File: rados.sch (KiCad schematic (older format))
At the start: 1 part

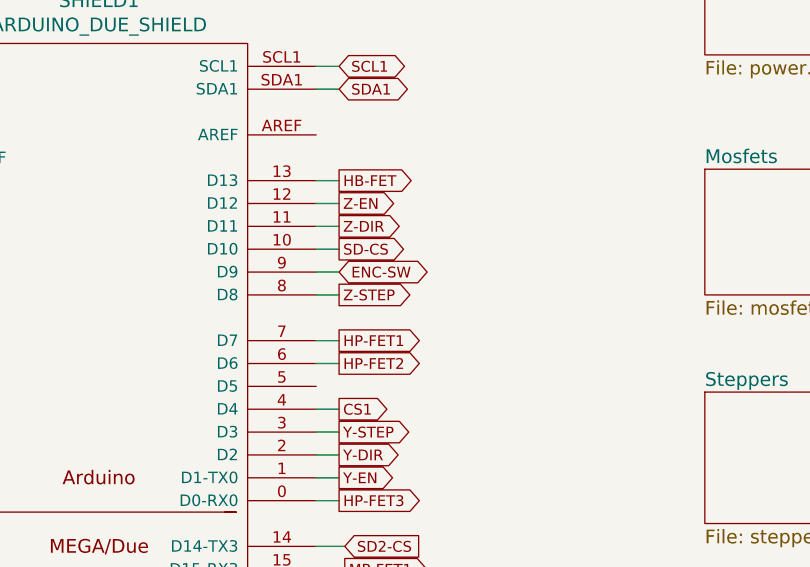
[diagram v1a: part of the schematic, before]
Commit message: Moved heatbed io away from arduino led-output (D13)
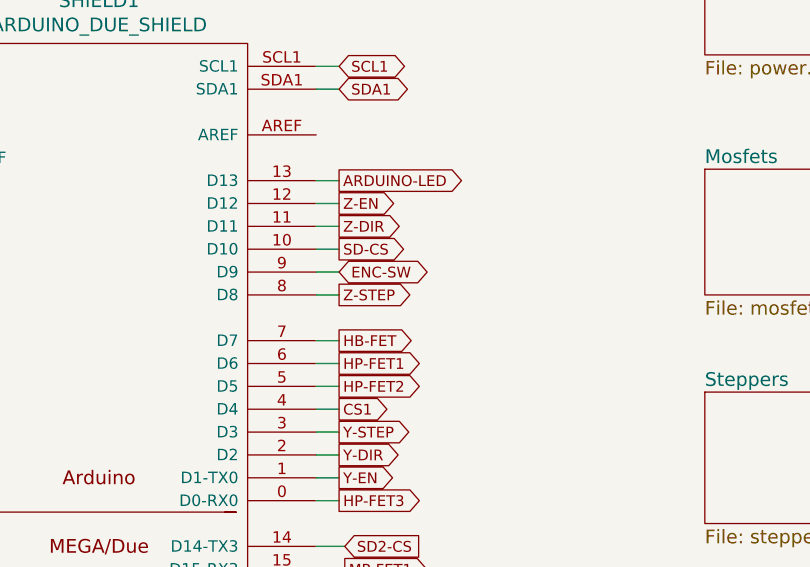
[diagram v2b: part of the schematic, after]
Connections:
- net labels added: ARDUINO-LED
- wire segments 79 -> 80
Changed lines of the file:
@@
 	1    0    0    -1
 $EndComp
-Wire Wire Line
-	2650 2300 3100 2300
 $Comp
 L +5V #PWR1
@@
 	1    0    0    -1
 $EndComp
-Wire Wire Line
-	2525 2400 3100 2400
 $Sheet
 S 6700 900  1025 550
@@
 F1 "mosfets.sch" 60
 $EndSheet
-Text GLabel 5100 2000 2    47   Output ~ 0
+Text GLabel 5100 2700 2    47   Output ~ 0
 HB-FET
-Text GLabel 5100 2700 2    47   Output ~ 0
+Text GLabel 5100 2800 2    47   Output ~ 0
 HP-FET1
-Text GLabel 5100 2800 2    47   Output ~ 0
+Text GLabel 5100 2900 2    47   Output ~ 0
 HP-FET2
 Text GLabel 5100 3400 2    47   Output ~ 0
@@
 Text GLabel 5125 4300 2    47   Output ~ 0
 LP-FET2
-Wire Wire Line
-	5000 2000 5100 2000
-Wire Wire Line
-	5000 2100 5100 2100
-Wire Wire Line
-	5000 2200 5100 2200
-Wire Wire Line
-	5000 2400 5100 2400
-Wire Wire Line
-	5000 2500 5100 2500
-Wire Wire Line
-	5000 3400 5100 3400
-Wire Wire Line
-	5100 2800 5000 2800
 $Sheet
 S 6700 2925 1050 575
@@
 Text GLabel 5100 3000 2    47   Output ~ 0
 CS1
-Wire Wire Line
-	5100 3000 5000 3000
-Wire Wire Line
-	5100 2300 5000 2300
 Text GLabel 5100 2200 2    47   Output ~ 0
 Z-DIR
 Text GLabel 5100 2500 2    47   Output ~ 0
 Z-STEP
-Wire Wire Line
-	5000 3100 5100 3100
-Wire Wire Line
-	5000 3200 5100 3200
 Text GLabel 5125 3600 2    47   Input ~ 0
 SD2-CS
@@
 	1    0    0    -1
 $EndComp
-Wire Wire Line
-	5125 3600 5000 3600
-Wire Wire Line
-	5125 3700 5000 3700
-Wire Wire Line
-	5125 3800 5000 3800
-Wire Wire Line
-	5125 3900 5000 3900
-Wire Wire Line
-	5000 4200 5125 4200
-Wire Wire Line
-	5125 4300 5000 4300
-Wire Wire Line
-	5000 4625 5000 4725
 Text GLabel 5100 3300 2    47   Output ~ 0
 Y-EN
@@
 Text GLabel 3000 6400 0    47   Input ~ 0
 Z+
-Wire Wire Line
-	5125 5050 5000 5050
-Wire Wire Line
-	5000 5250 5125 5250
-Wire Wire Line
-	5000 5450 5125 5450
-Wire Wire Line
-	5125 5150 5000 5150
-Wire Wire Line
-	5000 5550 5125 5550
-Wire Wire Line
-	5125 6000 5000 6000
-Wire Wire Line
-	5000 5350 5125 5350
-Wire Wire Line
-	5125 5650 5000 5650
-Wire Wire Line
-	5125 6200 5000 6200
 Text GLabel 5125 5900 2    47   BiDi ~ 0
 LCD-RS
@@
 Text GLabel 5125 5550 2    47   BiDi ~ 0
 ENC-A
-Wire Wire Line
-	2975 5550 3100 5550
-Wire Wire Line
-	3000 5300 3100 5300
-Wire Wire Line
-	3100 5100 3000 5100
 Text GLabel 2975 5950 0    47   Output ~ 0
 E3-EN
@@
 Text GLabel 2975 5750 0    47   Output ~ 0
 E3-DIR
-Wire Wire Line
-	3000 5000 3100 5000
-Wire Wire Line
-	3100 5200 3000 5200
-Wire Wire Line
-	3000 5450 3100 5450
 $Comp
 L GND #PWR4
@@
 	1    0    0    -1
 $EndComp
-Wire Wire Line
-	3100 4625 3100 4850
 Text GLabel 2975 3300 0    47   Output ~ 0
 E2-STEP
@@
 Text GLabel 2975 3200 0    47   Output ~ 0
 E2-DIR
-Wire Wire Line
-	2975 3400 3100 3400
-Wire Wire Line
-	3100 4000 3000 4000
-Wire Wire Line
-	3000 3900 3100 3900
 Text GLabel 2975 3000 0    47   Output ~ 0
 E1-STEP
@@
 Text GLabel 2975 2900 0    47   Output ~ 0
 E1-DIR
-Wire Wire Line
-	3000 3800 3100 3800
-Wire Wire Line
-	3100 3600 3000 3600
-Wire Wire Line
-	3000 3500 3100 3500
-Wire Wire Line
-	3000 2700 3100 2700
-Wire Wire Line
-	2650 2300 2650 2275
-Wire Wire Line
-	3000 2200 3100 2200
 Text GLabel 3000 4100 0    47   Input ~ 0
 T0
@@
 Text GLabel 3000 4500 0    47   Input ~ 0
 T4
-Wire Wire Line
-	3000 4500 3100 4500
-Wire Wire Line
-	3100 4400 3000 4400
-Wire Wire Line
-	3000 4300 3100 4300
-Wire Wire Line
-	3100 4200 3000 4200
-Wire Wire Line
-	3000 4100 3100 4100
 Text GLabel 5125 5350 2    47   Input ~ 0
 STATUS-LED
-Wire Wire Line
-	3000 6300 3100 6300
 Text GLabel 5100 1500 2    47   BiDi ~ 0
 SCL1
 Text GLabel 5100 1600 2    47   BiDi ~ 0
 SDA1
-Wire Wire Line
-	5100 1500 5000 1500
-Wire Wire Line
-	5000 1600 5100 1600
 Text GLabel 2975 1500 0    47   Input ~ 0
 SD-MISO
@@
 Text GLabel 2975 1700 0    47   Input ~ 0
 SD-SCK
-Wire Wire Line
-	2975 1500 3100 1500
-Wire Wire Line
-	3100 1600 2975 1600
-Wire Wire Line
-	2975 1700 3100 1700
-Connection ~ 3100 4725
-Connection ~ 3100 4825
-Connection ~ 5000 4625
-Wire Wire Line
-	5125 4100 5000 4100
-Wire Wire Line
-	5000 4000 5125 4000
-Wire Wire Line
-	5100 3300 5000 3300
 Text GLabel 3000 6300 0    47   Input ~ 0
 PROBE
-Wire Wire Line
-	5000 6400 5125 6400
-Wire Wire Line
-	5000 6500 5125 6500
-Wire Wire Line
-	3000 6400 3100 6400
-Wire Wire Line
-	3000 6600 3100 6600
-Wire Wire Line
-	5125 6600 5000 6600
-Wire Wire Line
-	5125 6300 5000 6300
 Text GLabel 3000 3600 0    47   BiDi ~ 0
 AUX-1
@@
 Text GLabel 3000 4000 0    47   BiDi ~ 0
 AUX-4
-Wire Wire Line
-	2975 2900 3100 2900
-Wire Wire Line
-	3100 3000 2975 3000
-Wire Wire Line
-	2975 3100 3100 3100
-Wire Wire Line
-	2975 3200 3100 3200
-Wire Wire Line
-	3100 3300 2975 3300
-Wire Wire Line
-	3000 6500 3100 6500
-Wire Wire Line
-	3100 6150 2975 6150
-Wire Wire Line
-	5125 5750 5000 5750
-Wire Wire Line
-	2975 5750 3100 5750
-Wire Wire Line
-	2975 5950 3100 5950
-Wire Wire Line
-	2975 5850 3100 5850
-Wire Wire Line
-	5100 2700 5000 2700
 Text GLabel 5125 3800 2    47   Output ~ 0
 ESP-RX
@@
 ESP-TX
 Wire Wire Line
+	2650 2300 3100 2300
+Wire Wire Line
+	2525 2400 3100 2400
+Wire Wire Line
+	5000 2700 5100 2700
+Wire Wire Line
+	5000 2100 5100 2100
+Wire Wire Line
+	5000 2200 5100 2200
+Wire Wire Line
+	5000 2400 5100 2400
+Wire Wire Line
+	5000 2500 5100 2500
+Wire Wire Line
+	5000 3400 5100 3400
+Wire Wire Line
+	5100 2900 5000 2900
+Wire Wire Line
+	5100 3000 5000 3000
+Wire Wire Line
+	5100 2300 5000 2300
+Wire Wire Line
+	5000 3100 5100 3100
+Wire Wire Line
+	5000 3200 5100 3200
+Wire Wire Line
+	5125 3600 5000 3600
+Wire Wire Line
+	5125 3700 5000 3700
+Wire Wire Line
+	5125 3800 5000 3800
+Wire Wire Line
+	5125 3900 5000 3900
+Wire Wire Line
+	5000 4200 5125 4200
+Wire Wire Line
+	5125 4300 5000 4300
+Wire Wire Line
+	5000 4625 5000 4725
+Wire Wire Line
+	5125 5050 5000 5050
+Wire Wire Line
+	5000 5250 5125 5250
+Wire Wire Line
+	5000 5450 5125 5450
+Wire Wire Line
+	5125 5150 5000 5150
+Wire Wire Line
+	5000 5550 5125 5550
+Wire Wire Line
+	5125 6000 5000 6000
+Wire Wire Line
+	5000 5350 5125 5350
+Wire Wire Line
+	5125 5650 5000 5650
+Wire Wire Line
+	5125 6200 5000 6200
+Wire Wire Line
+	2975 5550 3100 5550
+Wire Wire Line
+	3000 5300 3100 5300
+Wire Wire Line
+	3100 5100 3000 5100
+Wire Wire Line
+	3000 5000 3100 5000
+Wire Wire Line
+	3100 5200 3000 5200
+Wire Wire Line
+	3000 5450 3100 5450
+Wire Wire Line
+	3100 4625 3100 4850
+Wire Wire Line
+	2975 3400 3100 3400
+Wire Wire Line
+	3100 4000 3000 4000
+Wire Wire Line
+	3000 3900 3100 3900
+Wire Wire Line
+	3000 3800 3100 3800
+Wire Wire Line
+	3100 3600 3000 3600
+Wire Wire Line
+	3000 3500 3100 3500
+Wire Wire Line
+	3000 2700 3100 2700
+Wire Wire Line
+	2650 2300 2650 2275
+Wire Wire Line
+	3000 2200 3100 2200
+Wire Wire Line
+	3000 4500 3100 4500
+Wire Wire Line
+	3100 4400 3000 4400
+Wire Wire Line
+	3000 4300 3100 4300
+Wire Wire Line
+	3100 4200 3000 4200
+Wire Wire Line
+	3000 4100 3100 4100
+Wire Wire Line
+	3000 6300 3100 6300
+Wire Wire Line
+	5100 1500 5000 1500
+Wire Wire Line
+	5000 1600 5100 1600
+Wire Wire Line
+	2975 1500 3100 1500
+Wire Wire Line
+	3100 1600 2975 1600
+Wire Wire Line
+	2975 1700 3100 1700
+Connection ~ 3100 4725
+Connection ~ 3100 4825
+Connection ~ 5000 4625
+Wire Wire Line
+	5125 4100 5000 4100
+Wire Wire Line
+	5000 4000 5125 4000
+Wire Wire Line
+	5100 3300 5000 3300
+Wire Wire Line
+	5000 6400 5125 6400
+Wire Wire Line
+	5000 6500 5125 6500
+Wire Wire Line
+	3000 6400 3100 6400
+Wire Wire Line
+	3000 6600 3100 6600
+Wire Wire Line
+	5125 6600 5000 6600
+Wire Wire Line
+	5125 6300 5000 6300
+Wire Wire Line
+	2975 2900 3100 2900
+Wire Wire Line
+	3100 3000 2975 3000
+Wire Wire Line
+	2975 3100 3100 3100
+Wire Wire Line
+	2975 3200 3100 3200
+Wire Wire Line
+	3100 3300 2975 3300
+Wire Wire Line
+	3000 6500 3100 6500
+Wire Wire Line
+	3100 6150 2975 6150
+Wire Wire Line
+	5125 5750 5000 5750
+Wire Wire Line
+	2975 5750 3100 5750
+Wire Wire Line
+	2975 5950 3100 5950
+Wire Wire Line
+	2975 5850 3100 5850
+Wire Wire Line
+	5100 2800 5000 2800
+Wire Wire Line
 	5000 6100 5125 6100
 Wire Wire Line
 	5125 5900 5000 5900
+Text GLabel 5100 2000 2    47   Output ~ 0
+ARDUINO-LED
+Wire Wire Line
+	5000 2000 5100 2000
 $EndSCHEMATC

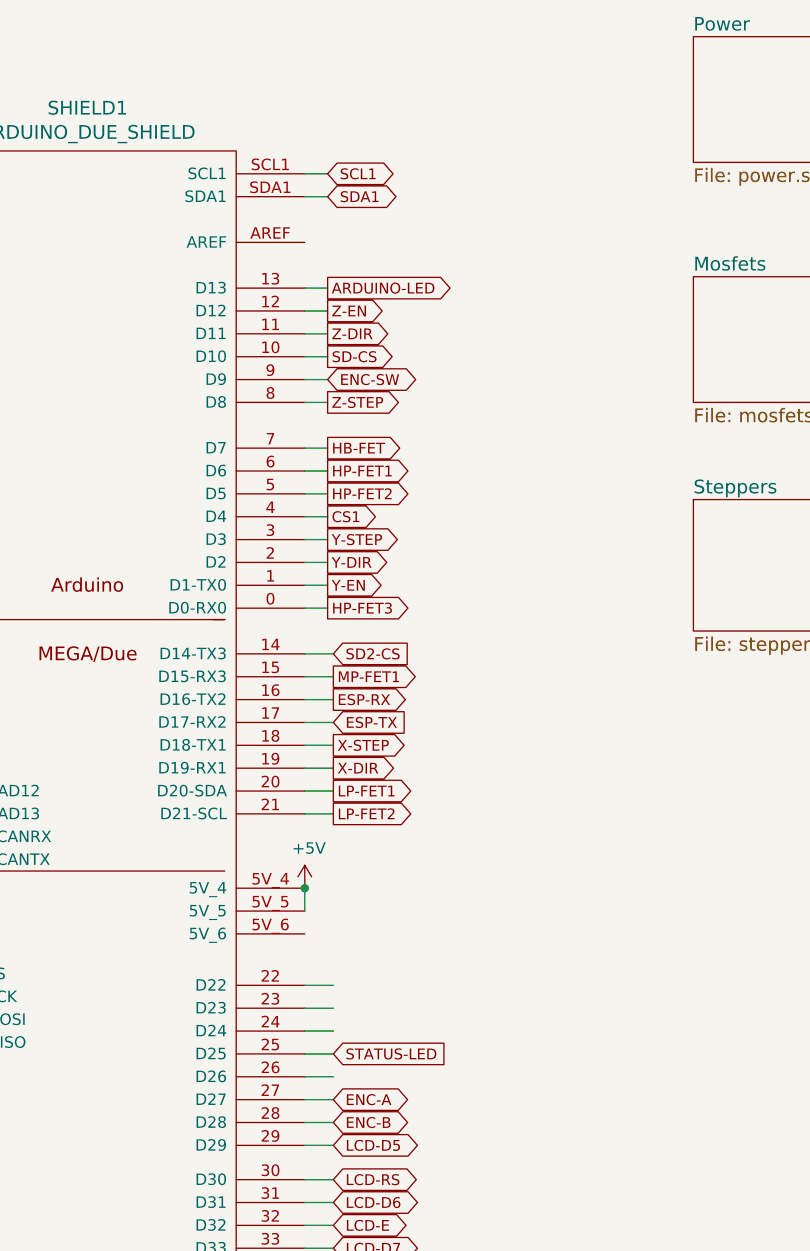
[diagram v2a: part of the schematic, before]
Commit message: - Some mosfets now can have hardware PWM - moved eeprom to i2c with arduino pull-ups
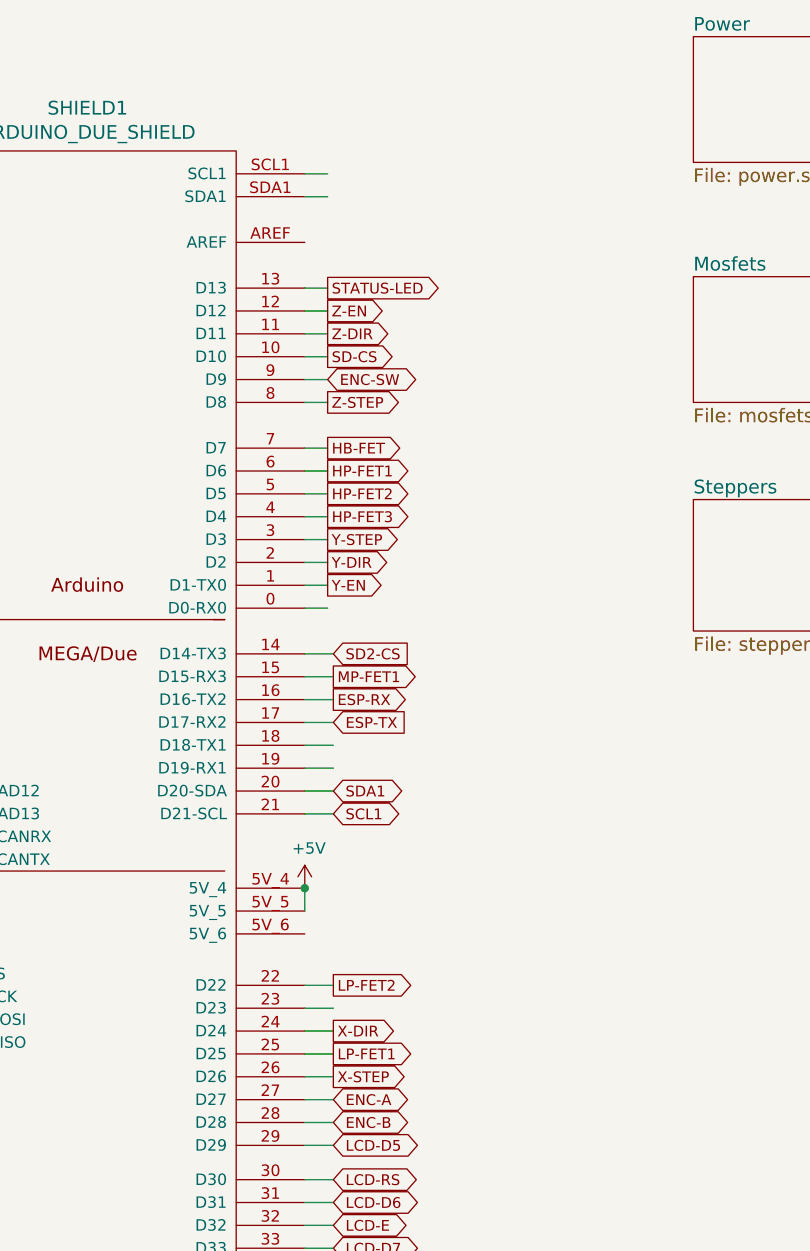
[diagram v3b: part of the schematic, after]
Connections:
- net labels removed: ARDUINO-LED, CS1
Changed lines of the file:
@@
 RESET
 $Comp
-L GND #PWR3
+L GND #PWR01
 U 1 1 568A9269
 P 3100 2500
-F 0 "#PWR3" H 3100 2250 50  0001 C CNN
+F 0 "#PWR01" H 3100 2250 50  0001 C CNN
 F 1 "GND" H 2975 2400 50  0000 C CNN
 F 2 "" H 3100 2500 50  0000 C CNN
@@
 $EndComp
 $Comp
-L +3.3V #PWR2
+L +3.3V #PWR02
 U 1 1 568A9448
 P 2650 2275
-F 0 "#PWR2" H 2650 2125 50  0001 C CNN
+F 0 "#PWR02" H 2650 2125 50  0001 C CNN
 F 1 "+3.3V" H 2625 2400 50  0000 C CNN
 F 2 "" H 2650 2275 50  0000 C CNN
@@
 $EndComp
 $Comp
-L +5V #PWR1
+L +5V #PWR03
 U 1 1 568A946E
 P 2525 2400
-F 0 "#PWR1" H 2525 2250 50  0001 C CNN
+F 0 "#PWR03" H 2525 2250 50  0001 C CNN
 F 1 "+5V" H 2500 2525 50  0000 C CNN
 F 2 "" H 2525 2400 50  0000 C CNN
@@
 Text GLabel 5100 2900 2    47   Output ~ 0
 HP-FET2
-Text GLabel 5100 3400 2    47   Output ~ 0
+Text GLabel 5100 3000 2    47   Output ~ 0
 HP-FET3
 Text GLabel 5125 3700 2    47   Output ~ 0
 MP-FET1
-Text GLabel 5125 4200 2    47   Output ~ 0
+Text GLabel 5125 5350 2    47   Output ~ 0
 LP-FET1
-Text GLabel 5125 4300 2    47   Output ~ 0
+Text GLabel 5125 5050 2    47   Output ~ 0
 LP-FET2
 $Sheet
@@
 Text GLabel 5100 2300 2    47   Output ~ 0
 SD-CS
-Text GLabel 5100 3000 2    47   Output ~ 0
-CS1
 Text GLabel 5100 2200 2    47   Output ~ 0
 Z-DIR
@@
 Y-STEP
 $Comp
-L +5V #PWR5
+L +5V #PWR04
 U 1 1 568ECF51
 P 5000 4625
-F 0 "#PWR5" H 5000 4475 50  0001 C CNN
+F 0 "#PWR04" H 5000 4475 50  0001 C CNN
 F 1 "+5V" H 5018 4799 50  0000 C CNN
 F 2 "" H 5000 4625 50  0000 C CNN
@@
 Text GLabel 5100 3300 2    47   Output ~ 0
 Y-EN
-Text GLabel 5125 4100 2    47   Output ~ 0
+Text GLabel 5125 5250 2    47   Output ~ 0
 X-DIR
-Text GLabel 5125 4000 2    47   Output ~ 0
+Text GLabel 5125 5450 2    47   Output ~ 0
 X-STEP
 Text GLabel 2975 6150 0    47   Output ~ 0
@@
 E3-DIR
 $Comp
-L GND #PWR4
+L GND #PWR05
 U 1 1 568EE3CA
 P 3100 4850
-F 0 "#PWR4" H 3100 4600 50  0001 C CNN
+F 0 "#PWR05" H 3100 4600 50  0001 C CNN
 F 1 "GND" H 3100 4700 50  0000 C CNN
 F 2 "" H 3100 4850 50  0000 C CNN
@@
 Text GLabel 3000 4500 0    47   Input ~ 0
 T4
-Text GLabel 5125 5350 2    47   Input ~ 0
+Text GLabel 5100 2000 2    47   Output ~ 0
 STATUS-LED
-Text GLabel 5100 1500 2    47   BiDi ~ 0
+Text GLabel 5125 4300 2    47   BiDi ~ 0
 SCL1
-Text GLabel 5100 1600 2    47   BiDi ~ 0
+Text GLabel 5125 4200 2    47   BiDi ~ 0
 SDA1
 Text GLabel 2975 1500 0    47   Input ~ 0
@@
 Wire Wire Line
 	5125 5900 5000 5900
-Text GLabel 5100 2000 2    47   Output ~ 0
-ARDUINO-LED
 Wire Wire Line
 	5000 2000 5100 2000

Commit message: Fixed some TODO's
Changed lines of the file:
@@
 RESET
 $Comp
-L GND #PWR01
+L GND #PWR3
 U 1 1 568A9269
 P 3100 2500
-F 0 "#PWR01" H 3100 2250 50  0001 C CNN
+F 0 "#PWR3" H 3100 2250 50  0001 C CNN
 F 1 "GND" H 2975 2400 50  0000 C CNN
 F 2 "" H 3100 2500 50  0000 C CNN
@@
 $EndComp
 $Comp
-L +3.3V #PWR02
+L +3.3V #PWR2
 U 1 1 568A9448
 P 2650 2275
-F 0 "#PWR02" H 2650 2125 50  0001 C CNN
+F 0 "#PWR2" H 2650 2125 50  0001 C CNN
 F 1 "+3.3V" H 2625 2400 50  0000 C CNN
 F 2 "" H 2650 2275 50  0000 C CNN
@@
 $EndComp
 $Comp
-L +5V #PWR03
+L +5V #PWR1
 U 1 1 568A946E
 P 2525 2400
-F 0 "#PWR03" H 2525 2250 50  0001 C CNN
+F 0 "#PWR1" H 2525 2250 50  0001 C CNN
 F 1 "+5V" H 2500 2525 50  0000 C CNN
 F 2 "" H 2525 2400 50  0000 C CNN
@@
 F1 "mosfets.sch" 60
 $EndSheet
+Text GLabel 5100 2400 2    47   Output ~ 0
+HB-FET
+Text GLabel 5100 2500 2    47   Output ~ 0
+HP-FET1
 Text GLabel 5100 2700 2    47   Output ~ 0
-HB-FET
+HP-FET2
 Text GLabel 5100 2800 2    47   Output ~ 0
-HP-FET1
+HP-FET3
+Text GLabel 5100 3000 2    47   Output ~ 0
+MP-FET1
 Text GLabel 5100 2900 2    47   Output ~ 0
-HP-FET2
-Text GLabel 5100 3000 2    47   Output ~ 0
-HP-FET3
-Text GLabel 5125 3700 2    47   Output ~ 0
-MP-FET1
-Text GLabel 5125 5350 2    47   Output ~ 0
 LP-FET1
-Text GLabel 5125 5050 2    47   Output ~ 0
+Text GLabel 5125 5150 2    47   Output ~ 0
 LP-FET2
 $Sheet
@@
 F1 "misc.sch" 60
 $EndSheet
-Text GLabel 5100 2300 2    47   Output ~ 0
+Text GLabel 5100 1500 2    47   Output ~ 0
 SD-CS
 Text GLabel 5100 2200 2    47   Output ~ 0
 Z-DIR
-Text GLabel 5100 2500 2    47   Output ~ 0
+Text GLabel 5100 2300 2    47   Output ~ 0
 Z-STEP
 Text GLabel 5125 3600 2    47   Input ~ 0
@@
 Y-STEP
 $Comp
-L +5V #PWR04
+L +5V #PWR5
 U 1 1 568ECF51
 P 5000 4625
-F 0 "#PWR04" H 5000 4475 50  0001 C CNN
+F 0 "#PWR5" H 5000 4475 50  0001 C CNN
 F 1 "+5V" H 5018 4799 50  0000 C CNN
 F 2 "" H 5000 4625 50  0000 C CNN
@@
 	1    0    0    -1
 $EndComp
-Text GLabel 5100 3300 2    47   Output ~ 0
+Text GLabel 5125 3700 2    47   Output ~ 0
 Y-EN
 Text GLabel 5125 5250 2    47   Output ~ 0
@@
 Text GLabel 5125 6200 2    47   BiDi ~ 0
 LCD-D7
-Text GLabel 5100 2400 2    47   BiDi ~ 0
+Text GLabel 5100 1600 2    47   BiDi ~ 0
 ENC-SW
 Text GLabel 5125 5650 2    47   BiDi ~ 0
@@
 E3-DIR
 $Comp
-L GND #PWR05
+L GND #PWR4
 U 1 1 568EE3CA
 P 3100 4850
-F 0 "#PWR05" H 3100 4600 50  0001 C CNN
+F 0 "#PWR4" H 3100 4600 50  0001 C CNN
 F 1 "GND" H 3100 4700 50  0000 C CNN
 F 2 "" H 3100 4850 50  0000 C CNN
